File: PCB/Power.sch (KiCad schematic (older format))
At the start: 15 parts, among them U5 AP2114, U6 SPX431, U7 ISA_DC-DC_converter

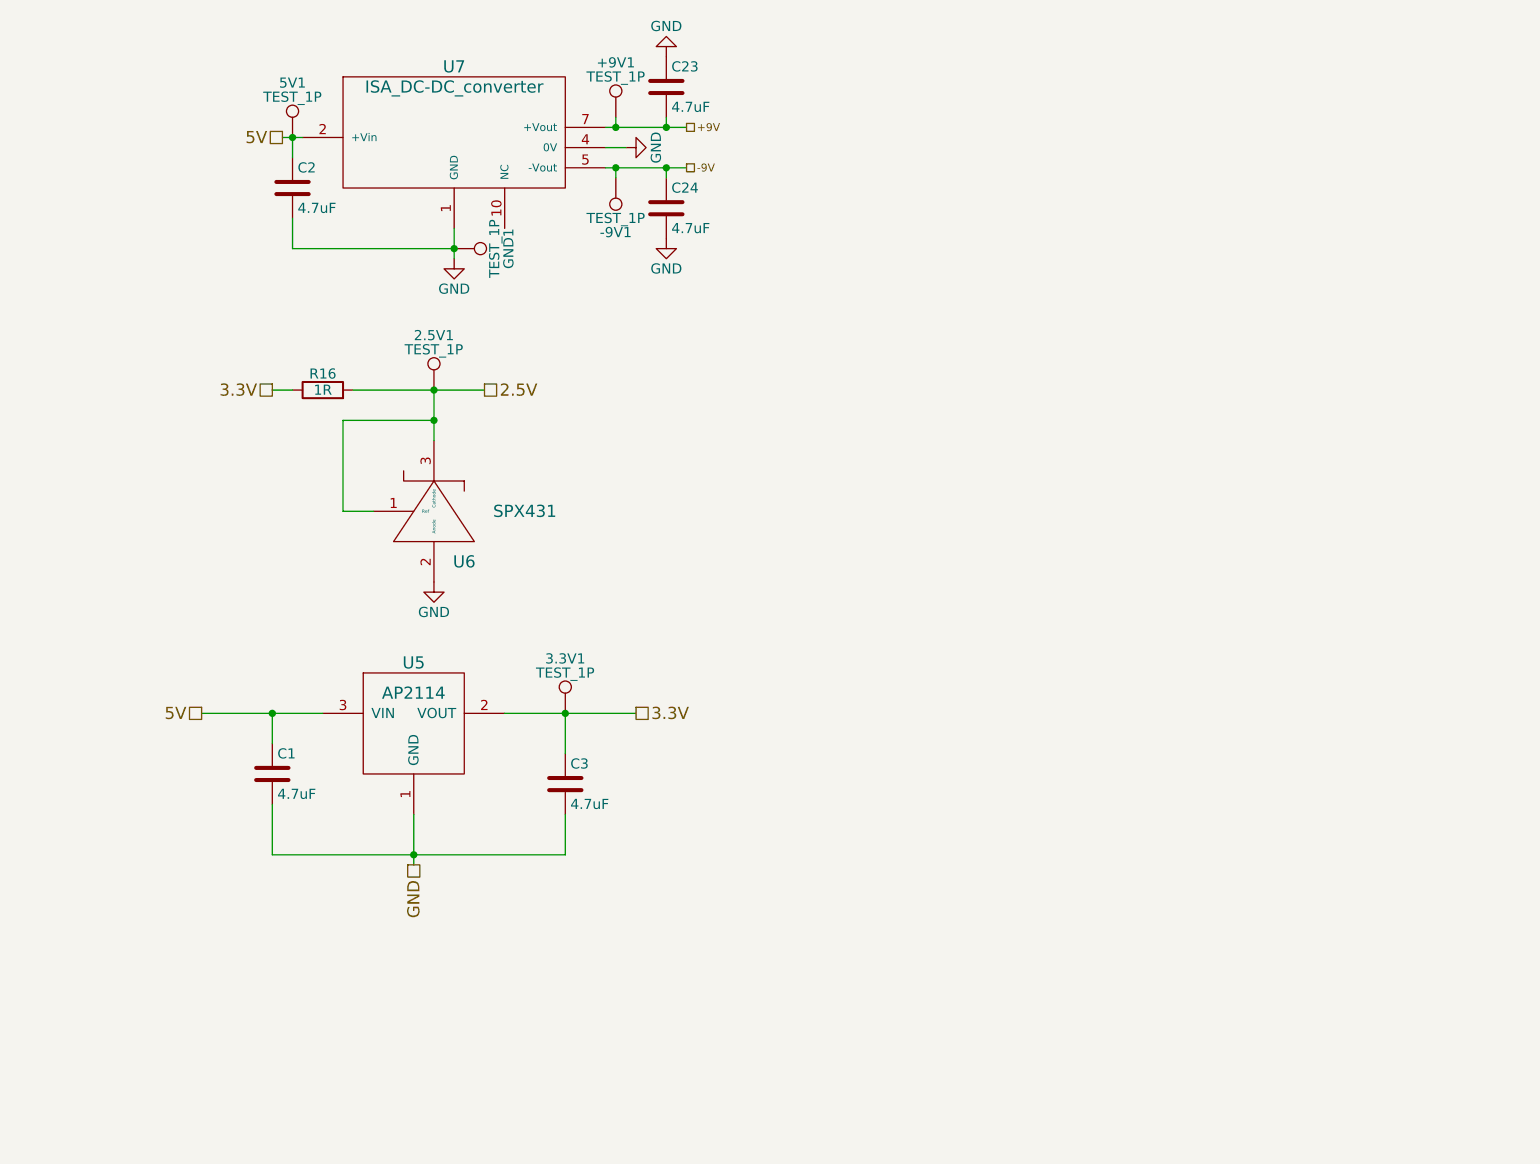
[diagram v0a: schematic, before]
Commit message: Generated BOM, fixed component names in schematic
Changed component names on output resistors and status LED to match that
in PCB
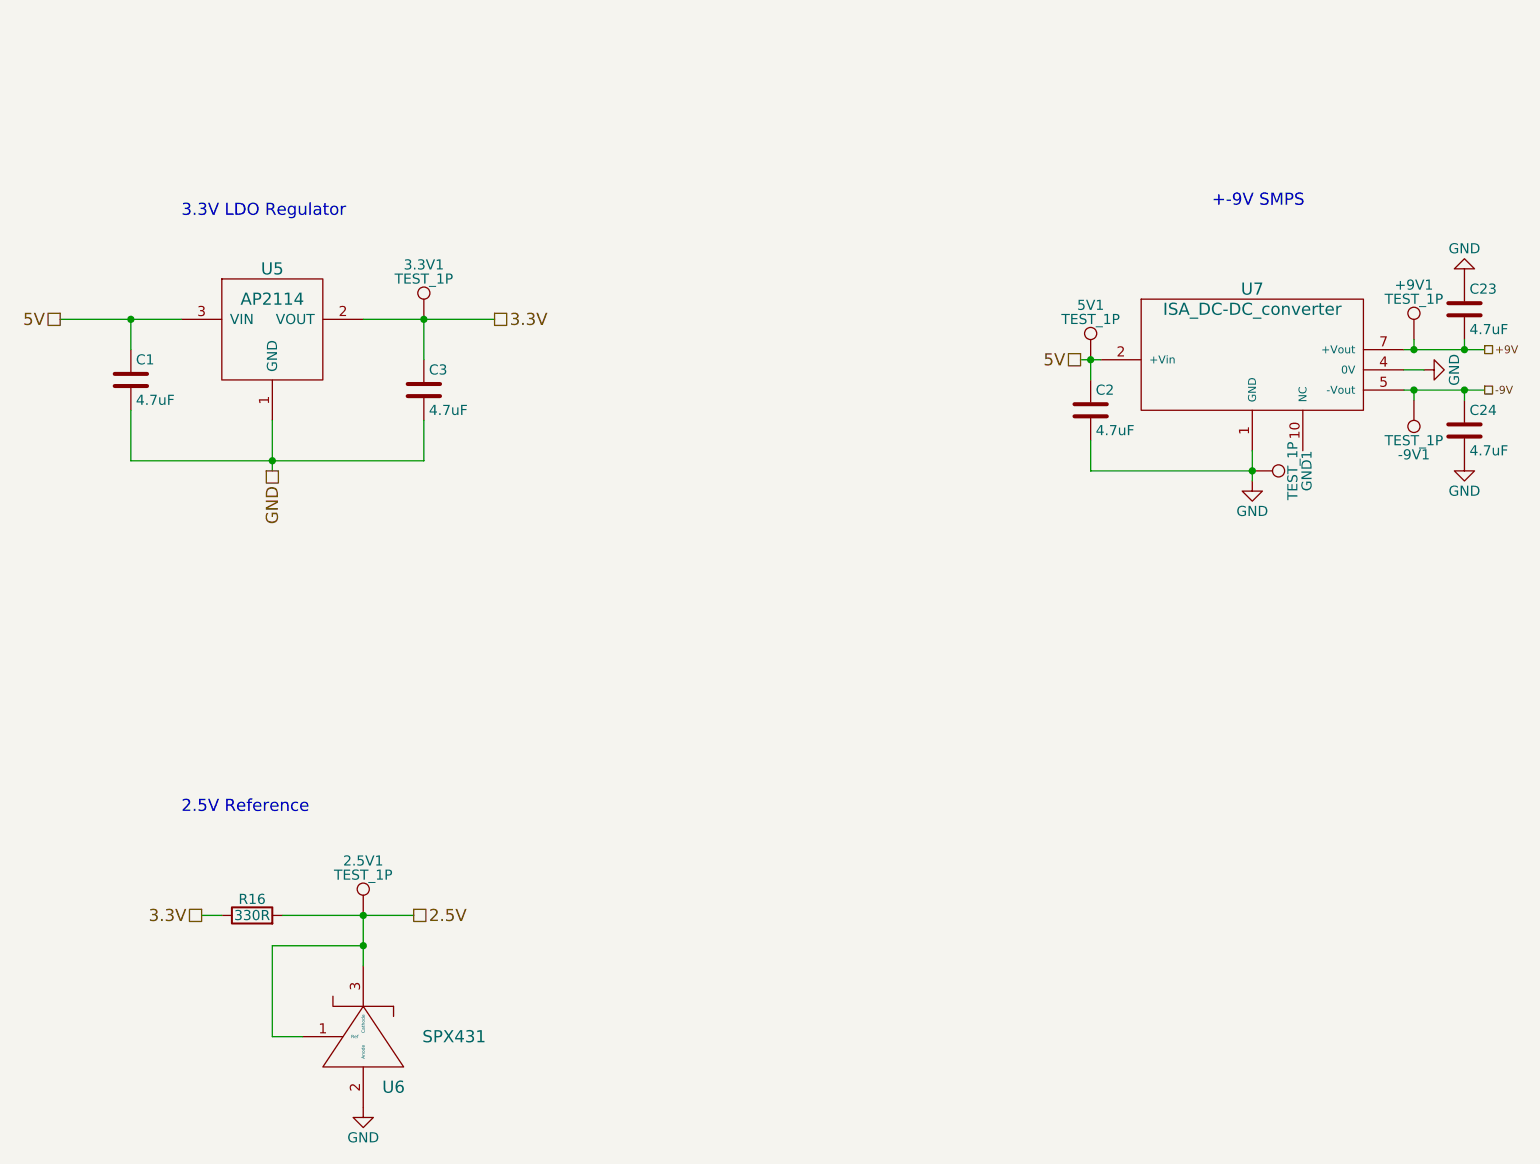
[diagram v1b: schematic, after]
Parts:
- R16: value 1R -> 330R
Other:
- note added: "+-9V SMPS\n"
- note added: "2.5V Reference\n"
- note added: "3.3V LDO Regulator\n"
- moved on the sheet: +9V1, -9V1, 2.5V1, 3.3V1, 5V1, C1, C2, C23, C24, C3, GND1, R16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

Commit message: Reannotated Components
Annotated components to standards,
TODO: Add Silkscreen for signals on bottom
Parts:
- renumbered C3 to C2, C2 to C3, C23 to C4, C24 to C5, U5 to U1, U6 to U2, U7 to U3
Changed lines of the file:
@@
 $EndDescr
 $Comp
-L AP2114 U5
+L AP2114 U1
 U 1 1 56B1EE67
 P 2650 2350
-F 0 "U5" H 2650 2700 60  0000 C CNN
+F 0 "U1" H 2650 2700 60  0000 C CNN
 F 1 "AP2114" H 2650 2550 60  0000 C CNN
 F 2 "TO_SOT_Packages_SMD:SOT-223" H 2650 2350 60  0001 C CNN
@@
 $EndComp
 $Comp
-L C C3
+L C C2
 U 1 1 56B1F1C7
 P 3400 2600
-F 0 "C3" H 3425 2700 50  0000 L CNN
+F 0 "C2" H 3425 2700 50  0000 L CNN
 F 1 "4.7uF" H 3425 2500 50  0000 L CNN
 F 2 "Capacitors_SMD:C_0603" H 3438 2450 50  0001 C CNN
@@
 	3100 5200 3100 5450
 $Comp
-L SPX431A,B,C U6
+L SPX431A,B,C U2
 U 1 1 56EC0B3D
 P 3100 5950
-F 0 "U6" H 3250 5850 60  0000 C CNN
+F 0 "U2" H 3250 5850 60  0000 C CNN
 F 1 "SPX431" H 3550 6100 60  0000 C CNN
 F 2 "TO_SOT_Packages_SMD:SOT89-3_Housing" H 3100 5950 60  0001 C CNN
@@
 	2400 5200 2300 5200
 $Comp
-L ISA_DC-DC_converter U7
+L ISA_DC-DC_converter U3
 U 1 1 56EC1847
 P 7500 2600
-F 0 "U7" H 7500 3100 60  0000 C CNN
+F 0 "U3" H 7500 3100 60  0000 C CNN
 F 1 "ISA_DC-DC_converter" H 7500 3000 60  0000 C CNN
 F 2 "Personal Library:SOIC-10" H 7500 2600 60  0001 C CNN
@@
 $EndComp
 $Comp
-L C C2
+L C C3
 U 1 1 5703D2C6
 P 6700 2700
-F 0 "C2" H 6725 2800 50  0000 L CNN
+F 0 "C3" H 6725 2800 50  0000 L CNN
 F 1 "4.7uF" H 6725 2600 50  0000 L CNN
 F 2 "Capacitors_SMD:c_elec_4x5.8" H 6738 2550 50  0001 C CNN
@@
 	6700 2850 6700 3000
 $Comp
-L C C24
+L C C5
 U 1 1 5703D6D6
 P 8550 2800
-F 0 "C24" H 8575 2900 50  0000 L CNN
+F 0 "C5" H 8575 2900 50  0000 L CNN
 F 1 "4.7uF" H 8575 2700 50  0000 L CNN
 F 2 "Capacitors_SMD:C_0603" H 8588 2650 50  0001 C CNN
@@
 $EndComp
 $Comp
-L C C23
+L C C4
 U 1 1 5703D915
 P 8550 2200
-F 0 "C23" H 8575 2300 50  0000 L CNN
+F 0 "C4" H 8575 2300 50  0000 L CNN
 F 1 "4.7uF" H 8575 2100 50  0000 L CNN
 F 2 "Capacitors_SMD:C_0603" H 8588 2050 50  0001 C CNN

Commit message: Replaced L1 footprint, changed Resistor values
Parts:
- R16: value 330R -> 150R
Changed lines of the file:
@@
 P 2550 5200
 F 0 "R16" V 2630 5200 50  0000 C CNN
-F 1 "330R" V 2550 5200 50  0000 C CNN
+F 1 "150R" V 2550 5200 50  0000 C CNN
 F 2 "Resistors_SMD:R_0805" V 2480 5200 50  0001 C CNN
 F 3 "" H 2550 5200 50  0000 C CNN
@@
 Text Notes 2200 1750 0    60   ~ 0
 3.3V LDO Regulator\n
-Text Notes 7300 1700 0    60   ~ 0
+Text Notes 7250 1900 0    60   ~ 0
 +-9V SMPS\n
-Text Notes 2200 4700 0    60   ~ 0
+Text Notes 2700 4700 0    60   ~ 0
 2.5V Reference\n
 $EndSCHEMATC

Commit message: Fixed schematic errors, "small" changes to PCB
Flipped DAC, changed component values, removed 1 capacitor, moved c16
from vref to power. Developed an urge to kill kicad
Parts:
- removed C2: 4.7uF, Capacitors_SMD:C_0603, symbol C
- added C2: 10uF, symbol CP1
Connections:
- net 3.3V: now also C2.1
- net GND: now also C2.2
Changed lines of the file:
@@
-	1    0    0    -1
-$EndComp
-$Comp
-L C C2
-U 1 1 56B1F1C7
-P 3400 2600
-F 0 "C2" H 3425 2700 50  0000 L CNN
-F 1 "4.7uF" H 3425 2500 50  0000 L CNN
-F 2 "Capacitors_SMD:C_0603" H 3438 2450 50  0001 C CNN
-F 3 "" H 3400 2600 50  0000 C CNN
-	1    3400 2600
 	1    0    0    -1
 $EndComp
@@
 Text Notes 2700 4700 0    60   ~ 0
 2.5V Reference\n
+$Comp
+L CP1 C2
+U 1 1 5713A8EC
+P 3400 2600
+F 0 "C2" H 3425 2700 50  0000 L CNN
+F 1 "10uF" H 3425 2500 50  0000 L CNN
+F 2 "" H 3400 2600 50  0000 C CNN
+F 3 "" H 3400 2600 50  0000 C CNN
+	1    3400 2600
+	1    0    0    -1
+$EndComp
 $EndSCHEMATC
